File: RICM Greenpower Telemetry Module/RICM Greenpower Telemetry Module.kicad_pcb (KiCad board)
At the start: 2 copper layers, 57.1 x 104.1 mm, 35 parts, among them J1 Conn_01x02_Female, J10 Conn_01x02_Female, J2 Conn_01x02_Female, J3 Conn_01x02_Female, J4 Jack-DC, J5 Conn_01x05_Female, J6 Conn_02x04_Counter_Clockwise, J7 Conn_01x03_Female, J8 Conn_01x03_Female, J9 Conn_01x04_Female, U1 Pico, U2 MPU_6050_module, U3 Adafruit_MicroSD_SPI_SDIO, U4 LTC2990

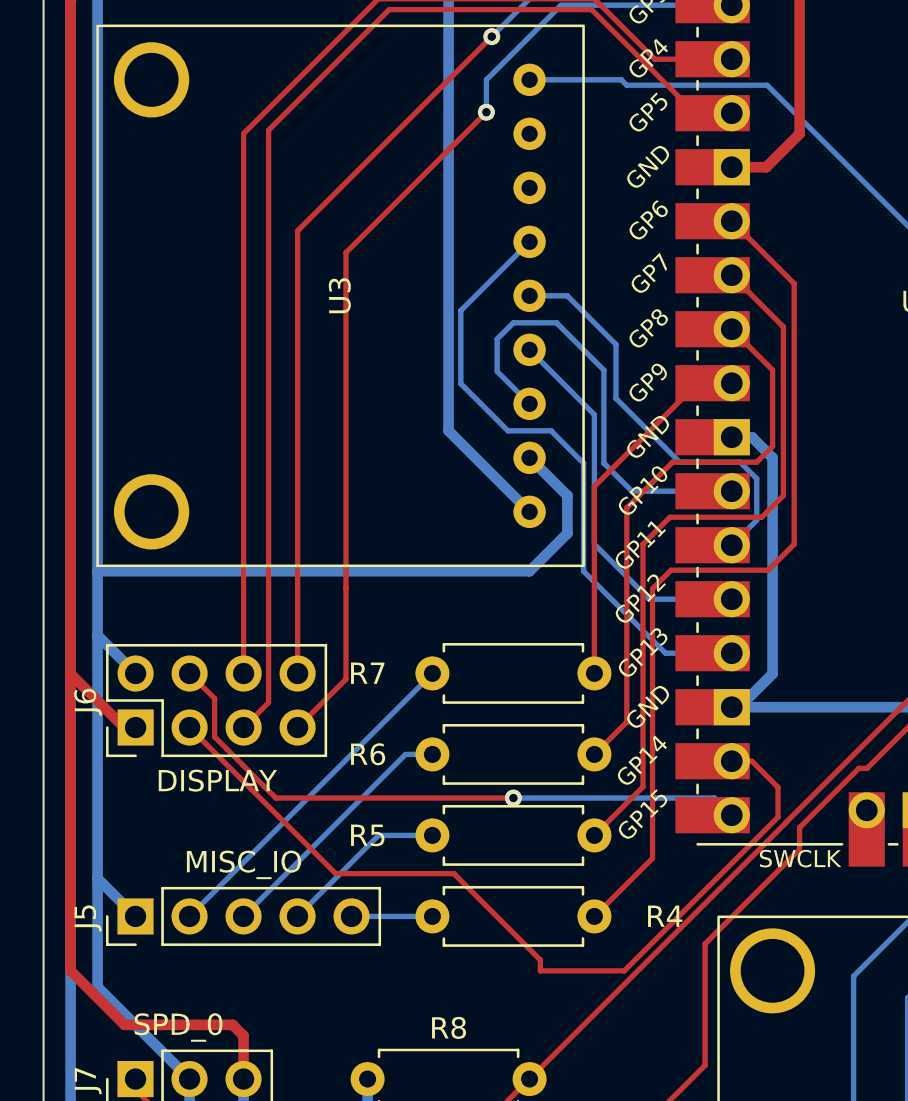
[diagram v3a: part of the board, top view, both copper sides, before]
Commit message: update cluster
Updated cluster schematic to use an I2C gpio expander. Added two pushbutton switches.
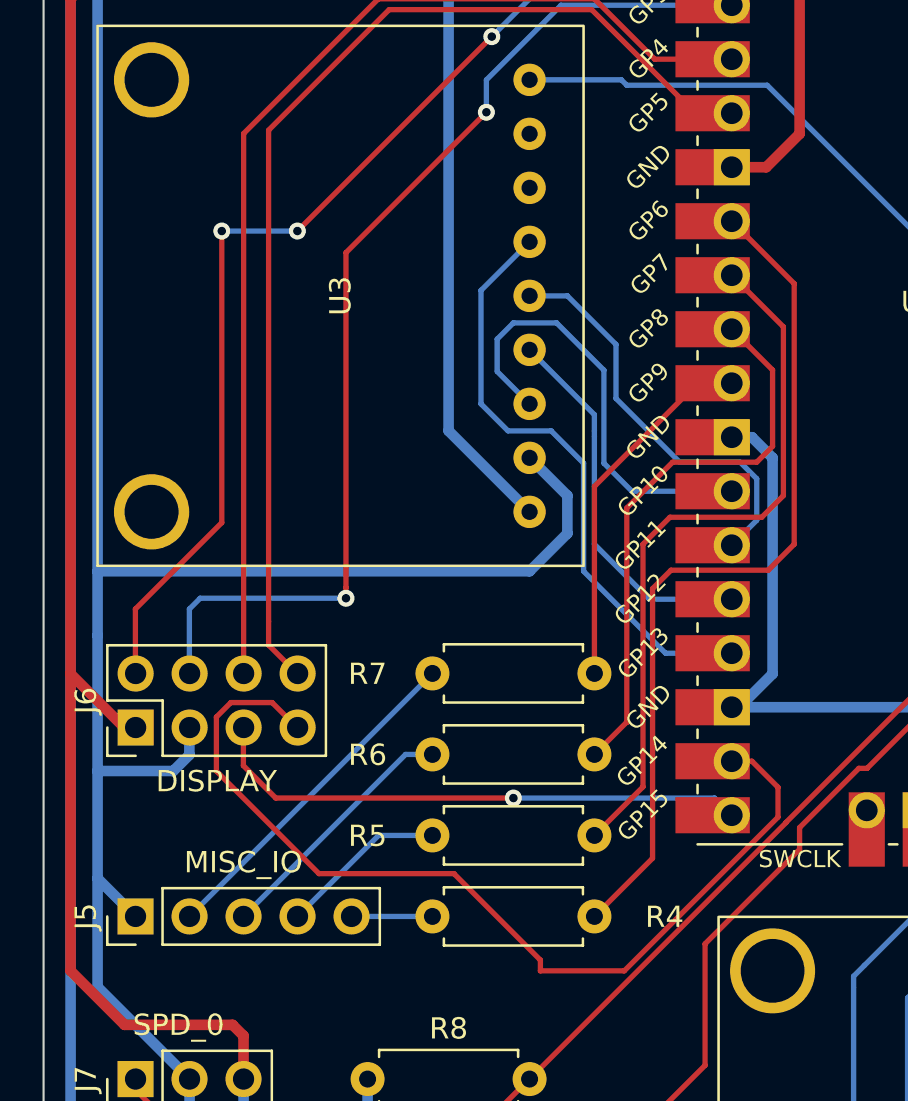
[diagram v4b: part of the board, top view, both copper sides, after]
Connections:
- J4 pad 3: GND -> (no net)
- J6 pad 3: I2C0_SDA -> I2C0_SCL
- J6 pad 4: I2C0_SCL -> I2C0_SDA
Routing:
- net Net-(J6-Pad8): track 46.7 -> 52.0 mm, vias 1 -> 3
- net I2C0_SDA: track 39.8 -> 44.8 mm
- net I2C0_SCL: track 29.3 -> 25.7 mm
- net Net-(J6-Pad7): track 47.1 -> 50.7 mm, vias 1 -> 2
- net GND: track 371.7 -> 375.1 mm
- net Net-(J6-Pad5): track 54.7 -> 52.3 mm
- net SD_CS: track 29.0 -> 28.2 mm

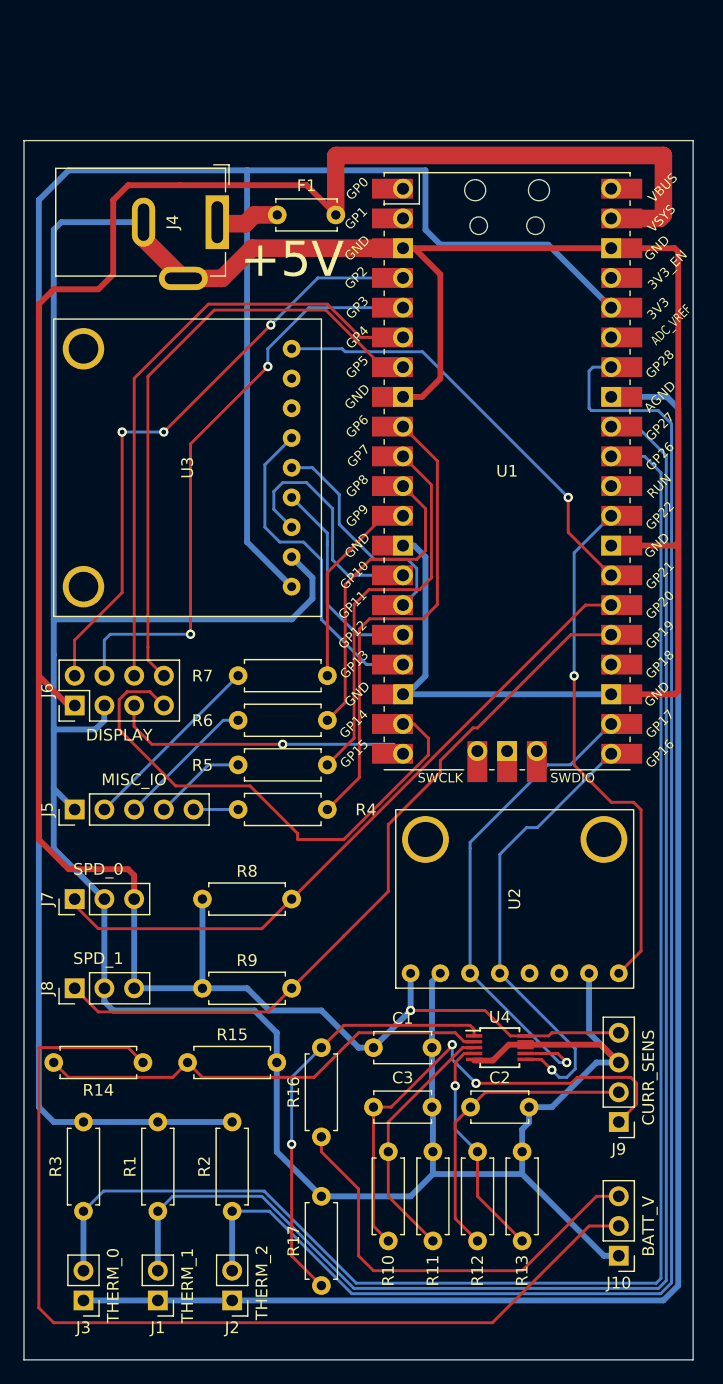
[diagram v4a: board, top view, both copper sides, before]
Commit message: added onboard regulator
Added onboard regulator and associated components. Added 4th thermistor connector.
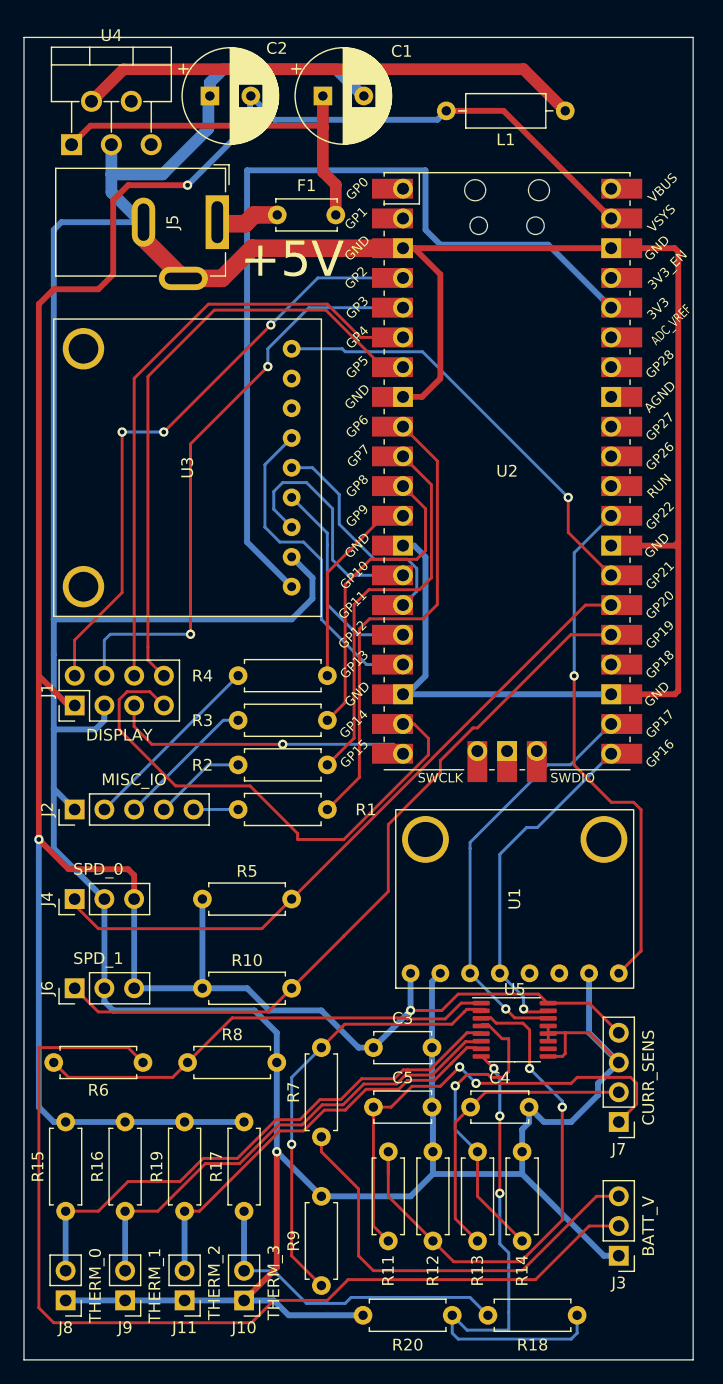
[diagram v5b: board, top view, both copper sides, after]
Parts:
- added C1: C, Capacitor_THT:CP_Radial_D8.0mm_P3.50mm, F.Cu at (38.2, 8.89)
- added C2: C, Capacitor_THT:CP_Radial_D8.0mm_P3.50mm, F.Cu at (28.6, 8.89)
- added J10: Conn_01x02_Female, Connector_PinHeader_2.54mm:PinHeader_1x02_P2.54mm_Vertical, F.Cu at (31.5, 111.8)
- added L1: L, Inductor_THT:L_Axial_L6.6mm_D2.7mm_P10.16mm_Horizontal_Vishay_IM-2, F.Cu at (58.9, 10.2)
- added R17: 10k, Resistor_THT:R_Axial_DIN0207_L6.3mm_D2.5mm_P7.62mm_Horizontal, F.Cu at (31.5, 104.1)
- added R18: 10k, Resistor_THT:R_Axial_DIN0207_L6.3mm_D2.5mm_P7.62mm_Horizontal, F.Cu at (52.3, 113.0)
- added R20: 10k, Resistor_THT:R_Axial_DIN0207_L6.3mm_D2.5mm_P7.62mm_Horizontal, F.Cu at (41.7, 113.0)
- added U5: ADS7830, Package_SO:TSSOP-16_4.4x5mm_P0.65mm, F.Cu at (54.6, 88.6)
- U4: value LTC2990 -> SI-8050TFE; footprint Package_SO:MSOP-10_3x3mm_P0.5mm -> Package_TO_SOT_THT:TO-220-5_P3.4x3.7mm_StaggerOdd_Lead3.8mm_Vertical
- moved U4 85.4 mm to (16.8, 13.0)
- moved J11 4.06 mm to (26.4, 111.8)
- moved R19 4.06 mm to (26.4, 104.1)
- moved J9 2.79 mm to (21.3, 111.8)
- moved R16 2.79 mm to (21.3, 104.1)
- moved J8 1.52 mm to (16.3, 111.8)
- moved R15 1.52 mm to (16.3, 104.1)
- renumbered C1 to C3, C2 to C4, C3 to C5, J6 to J1, J2 to J11, J5 to J2, J10 to J3, J7 to J4, J4 to J5, J8 to J6, J9 to J7, J3 to J8, J1 to J9, R4 to R1, R9 to R10, R10 to R11, R11 to R12, R12 to R13, R13 to R14, R3 to R15, R1 to R16, R2 to R19, R5 to R2, R6 to R3, R7 to R4, R8 to R5, R14 to R6, R16 to R7, R15 to R8, R17 to R9, U2 to U1, U1 to U2
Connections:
- F1 pad 2: +5V -> Net-(C1-Pad1)
- J11 pad 1: AGND -> GND
- J5 pad 3: (no net) -> GND
- J8 pad 1: AGND -> GND
- J9 pad 1: AGND -> GND
- R11 pad 2: Net-(R10-Pad2) -> Net-(R11-Pad2)
- R12 pad 1: Net-(R10-Pad2) -> Net-(R11-Pad2)
- R13 pad 2: Net-(R12-Pad2) -> Net-(R13-Pad2)
- R14 pad 1: Net-(R12-Pad2) -> Net-(R13-Pad2)
- R15 pad 2: +3V3 -> +5V
- R16 pad 2: +3V3 -> +5V
- R19 pad 2: +3V3 -> +5V
- R6 pad 2: Net-(R14-Pad2) -> Net-(R6-Pad2)
- R7 pad 2: Net-(R16-Pad2) -> Net-(R7-Pad2)
- R8 pad 1: Net-(R14-Pad2) -> Net-(R6-Pad2)
- R9 pad 1: Net-(R16-Pad2) -> Net-(R7-Pad2)
- U2 pad 31: THERM_0 -> unconnected-(U2-Pad31)
- U2 pad 32: THERM_1 -> unconnected-(U2-Pad32)
- U2 pad 33: AGND -> unconnected-(U2-Pad33)
- U2 pad 34: THERM_2 -> unconnected-(U2-Pad34)
- U4 pad 1: Net-(R16-Pad2) -> Net-(C1-Pad1)
- U4 pad 2: Net-(R14-Pad2) -> Net-(L1-Pad1)
- U4 pad 3: Net-(R10-Pad2) -> GND
- U4 pad 4: Net-(R12-Pad2) -> unconnected-(U4-Pad4)
- U4 pad 5: GND -> unconnected-(U4-Pad5)
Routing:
- net AGND: track 132.4 -> 0.00 mm
- net +3V3: track 189.4 -> 76.1 mm
- net THERM_2: track 132.1 -> 35.8 mm
- net THERM_1: track 128.8 -> 41.6 mm
- net THERM_0: track 132.2 -> 47.0 mm
- net GND: track 375.1 -> 451.1 mm, vias 0 -> 1
- net Net-(R11-Pad2): track 0.00 -> 46.3 mm, vias 0 -> 2
- net THERM_3: track 0.00 -> 43.8 mm, vias 0 -> 3
- net Net-(L1-Pad1): track 0.00 -> 43.1 mm
- net Net-(R6-Pad2): track 0.00 -> 39.6 mm
- net Net-(R14-Pad2): track 39.4 -> 0.00 mm
- net Net-(R7-Pad2): track 0.00 -> 37.8 mm, vias 0 -> 1
- net Net-(R16-Pad2): track 37.0 -> 0.00 mm, vias 1 -> 0
- net Net-(C1-Pad1): track 0.00 -> 32.8 mm
- net +5V: track 202.6 -> 233.5 mm, vias 1 -> 3
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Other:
- board size 57.1 x 104.1 mm -> 57.1 x 113 mm
- board text added: "THERM_3"

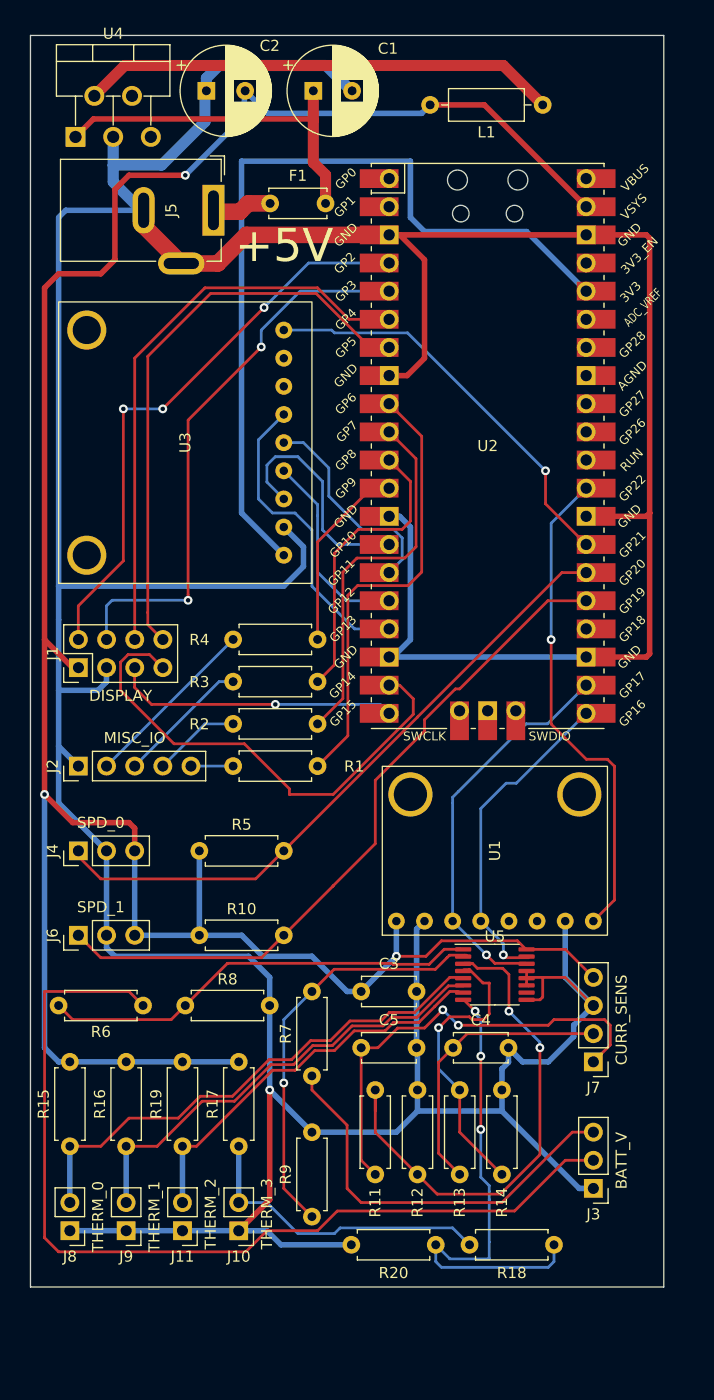
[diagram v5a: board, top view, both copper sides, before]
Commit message: rearranged board to fit regulator
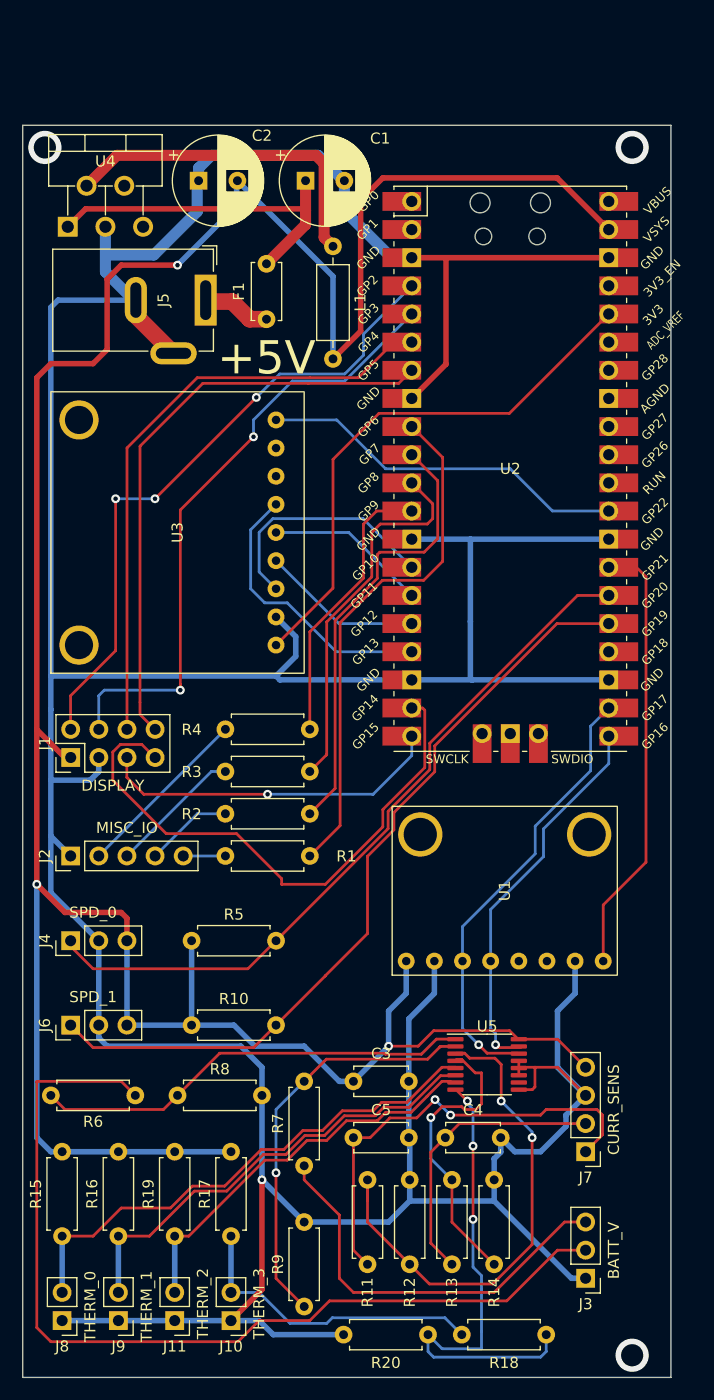
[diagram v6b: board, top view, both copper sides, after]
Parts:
- moved L1 22.8 mm to (40.0, 22.9), turned to -90 degrees
- moved F1 10.5 mm to (34.0, 29.5), turned to 90 degrees
- moved J3 8.14 mm to (62.8, 116.1)
- moved J1 8.14 mm to (16.3, 69.1)
- moved R4 8.14 mm to (30.3, 66.5)
- moved C1 8.14 mm to (37.5, 17.0)
- moved C3 8.14 mm to (41.8, 98.3)
- moved C4 8.14 mm to (50.1, 103.4)
- moved C5 8.14 mm to (41.8, 103.4)
- moved J7 8.14 mm to (62.8, 104.6)
- moved J8 8.14 mm to (15.6, 119.9)
- moved R10 8.14 mm to (27.2, 93.2)
- moved R12 8.14 mm to (46.9, 114.8)
- moved R13 8.14 mm to (50.7, 114.8)
- moved R15 8.14 mm to (15.6, 112.2)
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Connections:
- U2 pad 27: SD_DET -> ACC_INT
- U2 pad 29: ACC_INT -> SD_DET
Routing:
- net +5V: track 233.5 -> 263.1 mm
- net GND: track 451.1 -> 422.1 mm
- net +3V3: track 76.1 -> 49.2 mm
- net Net-(L1-Pad1): track 43.1 -> 30.7 mm
- net Net-(R4-Pad2): track 17.3 -> 25.4 mm
- net SPD_1: track 64.0 -> 71.6 mm
- net SPD_0: track 58.6 -> 66.2 mm
- net ACC_INT: track 44.7 -> 37.3 mm, vias 1 -> 0
- net Net-(R3-Pad2): track 26.6 -> 33.9 mm
- net Net-(R2-Pad2): track 33.6 -> 40.5 mm
- net Net-(R1-Pad2): track 40.5 -> 47.1 mm
- net I2C0_SDA: track 44.8 -> 51.2 mm
- net Net-(J1-Pad8): track 52.0 -> 58.3 mm
- net I2C0_SCL: track 25.7 -> 31.3 mm
- net I2C_SDA: track 29.5 -> 34.8 mm
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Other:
- board size 57.1 x 113 mm -> 58.5 x 113 mm

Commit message: tightened up spacing on the board
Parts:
- removed F1: Polyfuse, Capacitor_THT:C_Disc_D5.0mm_W2.5mm_P5.00mm
- removed the U4 at (16.1, 21.2)
- added C1: C, Capacitor_THT:C_Disc_D5.0mm_W2.5mm_P5.00mm, F.Cu at (28.5, 19.5)
- added U1: XL2001E1, Package_SO:SO-8_5.3x6.2mm_P1.27mm, F.Cu at (34.5, 26.5)
- moved C2 18.7 mm to (18.8, 17.2)
- moved C3 5.97 mm to (33.8, 17.0)
- renumbered C1 to C2, C2 to C3, C3 to C4, C4 to C5, C5 to C6, J5 to J1, J3 to J11, J1 to J3, J6 to J5, J9 to J6, J11 to J7, J7 to J9, R11 to R10, R12 to R11, R13 to R12, R14 to R13, R18 to R14, R20 to R15, R17 to R16, R6 to R17, R8 to R18, R7 to R19, R9 to R20, R10 to R6, R16 to R7, R19 to R8, R15 to R9, U1 to U3, U3 to U4
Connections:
- C2 pad 1: Net-(C1-Pad1) -> Net-(C1-Pad2)
- J1 pad 1: Net-(F1-Pad1) -> Net-(C1-Pad2)
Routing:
- net Net-(C1-Pad2): track 0.00 -> 36.1 mm
- net Net-(L1-Pad1): track 30.7 -> 4.90 mm
- net Net-(C1-Pad1): track 31.1 -> 21.4 mm
- net Net-(F1-Pad1): track 5.96 -> 0.00 mm
- net Net-(R10-Pad2): track 46.3 -> 44.4 mm
- net GND: track 422.1 -> 421.1 mm
- net +5V: track 263.1 -> 262.6 mm, vias 3 -> 2

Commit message: last revisions before first order
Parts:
- added C7: C, Capacitor_THT:C_Disc_D5.0mm_W2.5mm_P5.00mm, F.Cu at (62.0, 99.5)
- added C8: C, Capacitor_THT:C_Disc_D5.0mm_W2.5mm_P5.00mm, F.Cu at (62.0, 96.5)
- moved J11 6.20 mm to (69.0, 116.0)
- moved J9 5.70 mm to (68.5, 104.6)
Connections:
- U5 pad 10: unconnected-(U5-Pad10) -> +5V
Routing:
- net +5V: track 262.6 -> 298.1 mm
- net GND: track 421.1 -> 440.5 mm
- net Net-(J11-Pad2): track 85.1 -> 91.3 mm
- net Net-(J11-Pad3): track 36.9 -> 43.0 mm
- net Net-(C5-Pad1): track 25.9 -> 31.7 mm
- net Net-(C6-Pad1): track 40.8 -> 46.2 mm
- net (no net): vias 3 -> 4
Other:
- board size 58.5 x 113 mm -> 62.5 x 119 mm
